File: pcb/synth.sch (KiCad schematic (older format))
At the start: 50 parts, among them J1 Conn_01x06, SW1 SW_Push, SW10 SW_Push, SW11 SW_Push, SW12 SW_Push, SW13 SW_Push, SW14 SW_Push, SW15 SW_Push, SW16 SW_Push, SW17 SW_Push, SW18 SW_Push, SW19 SW_Push, SW2 SW_Push, SW20 SW_Push, SW21 SW_Push, SW22 SW_Push, SW23 SW_Push, SW24 SW_Push, SW3 SW_Push, SW4 SW_Push, SW5 SW_Push, SW6 SW_Push, SW7 SW_Push, SW8 SW_Push, SW9 SW_Push, U1 STM32F407VGTx, Y1 Crystal_8

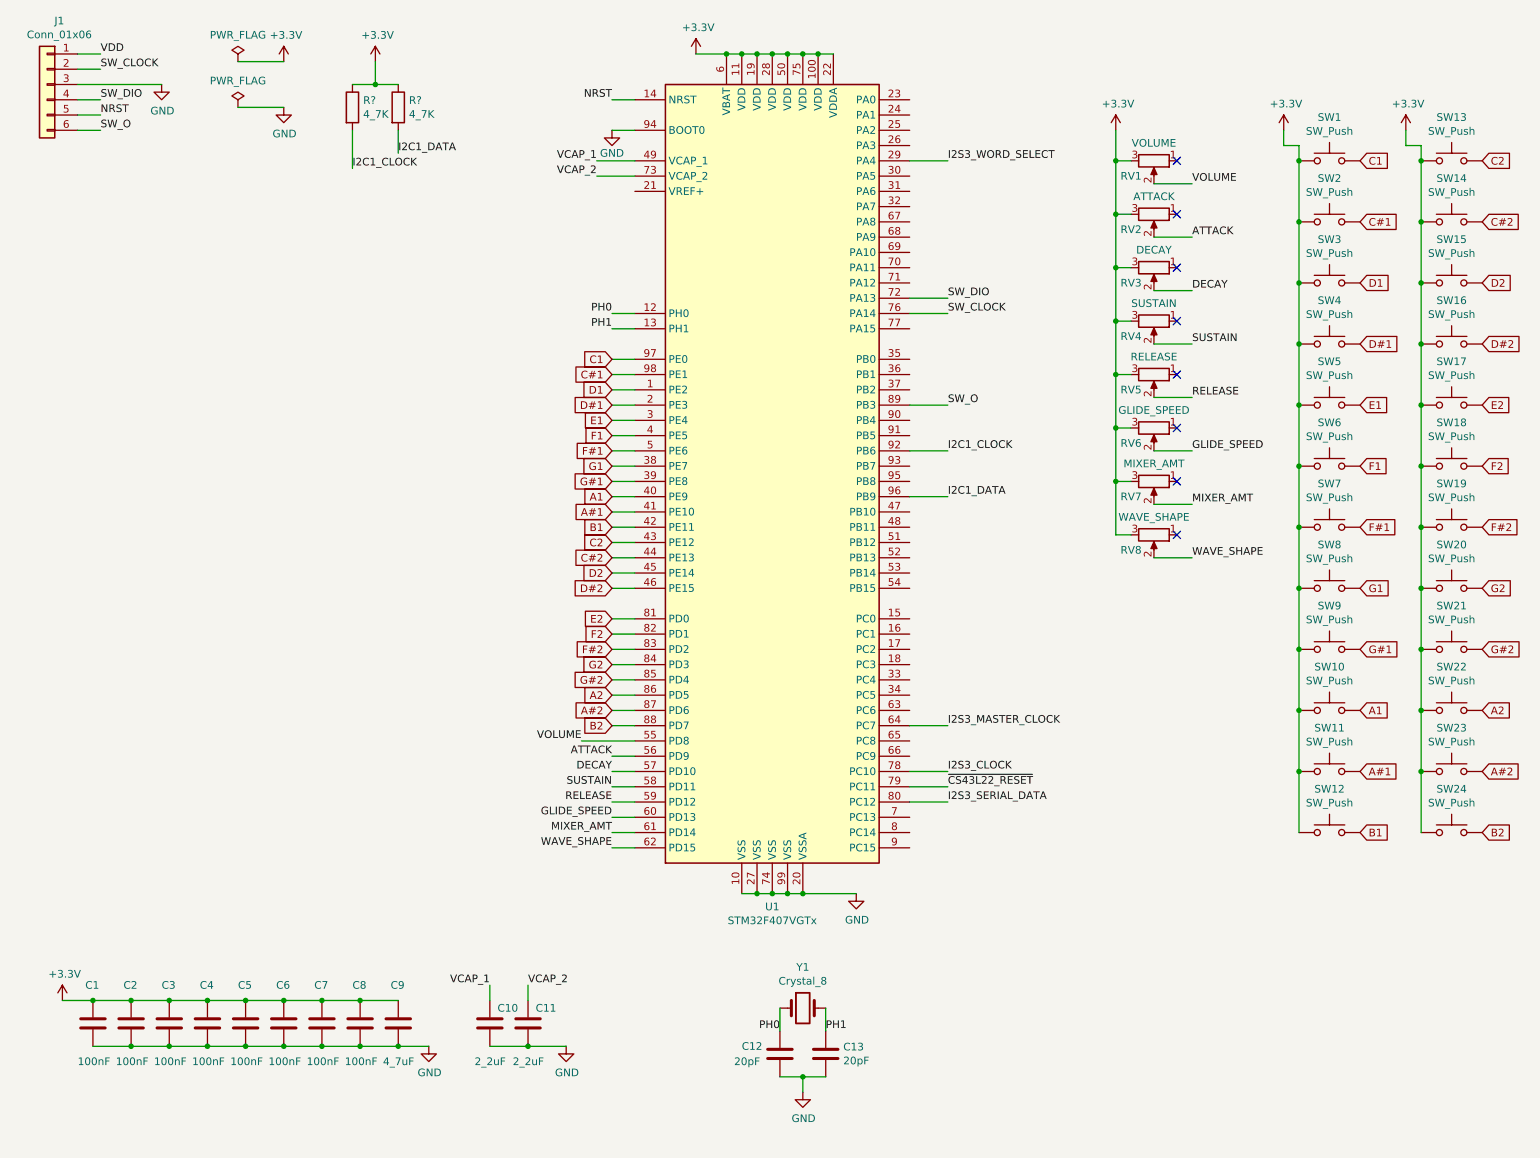
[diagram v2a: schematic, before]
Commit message: Add more buttons, and connect SWD VDD to 3.3V.
Also set some cap and resistor values.
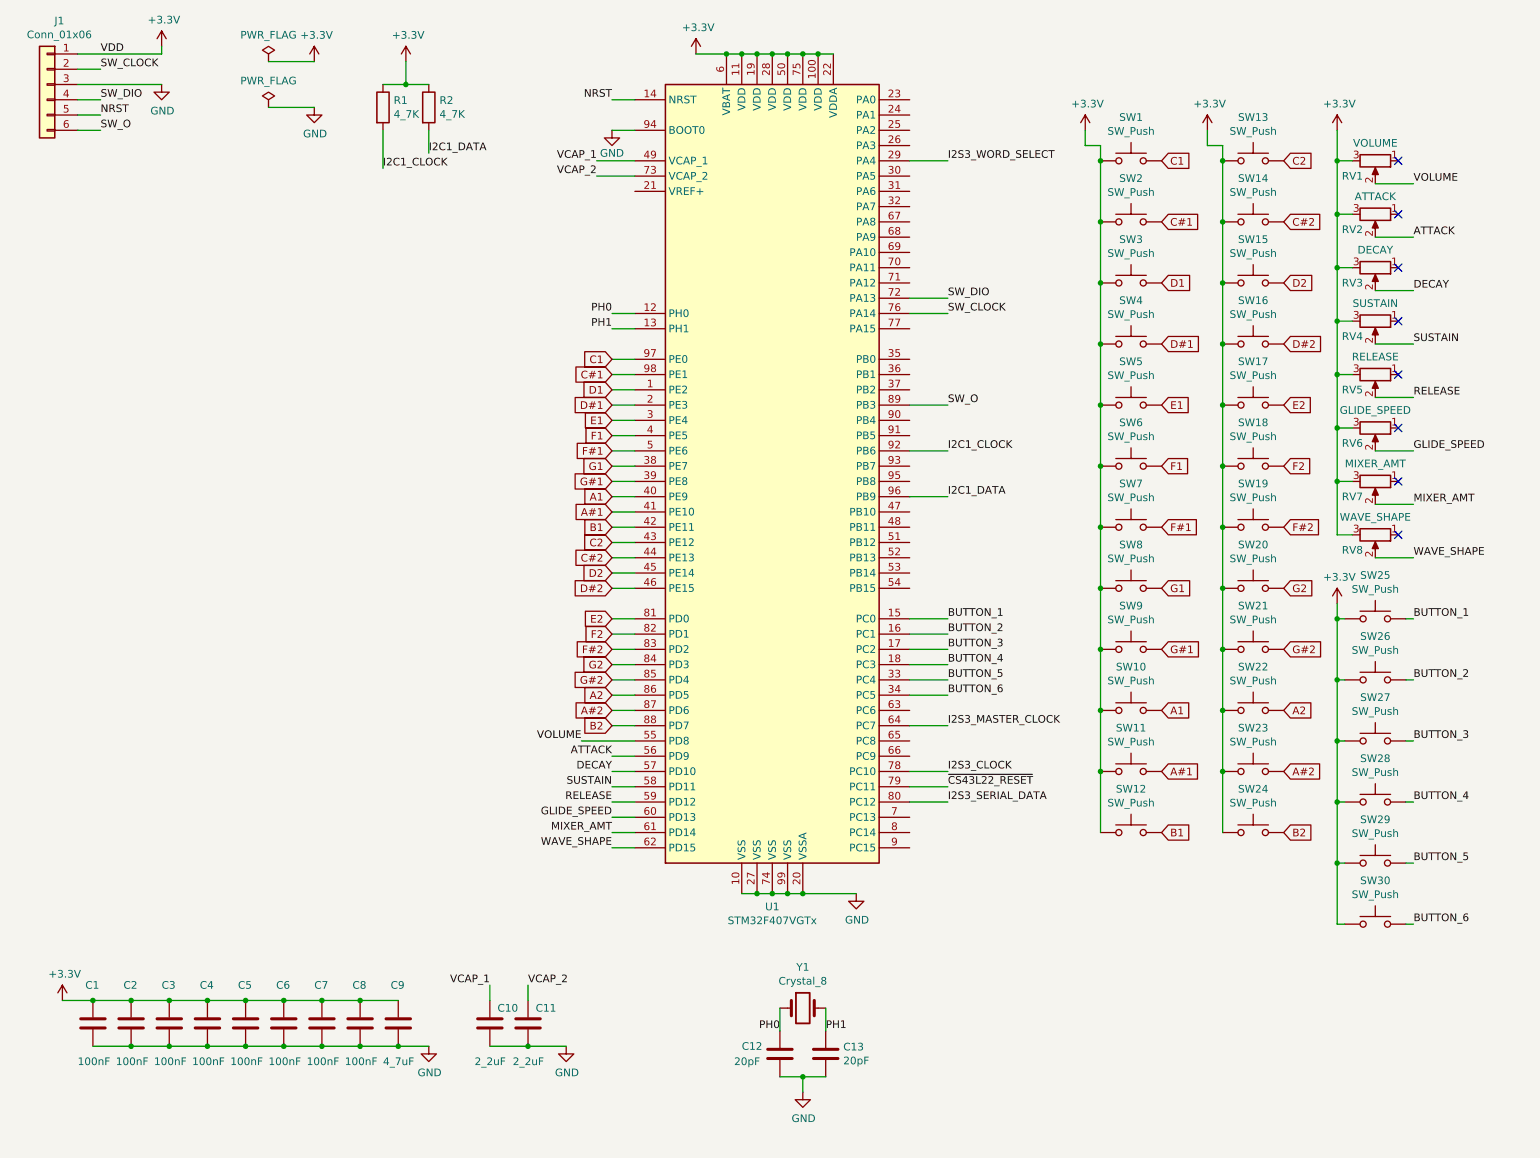
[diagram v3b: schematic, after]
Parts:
- added SW25, SW26, SW27, SW28, SW29, SW30: SW_Push, symbol Switch:SW_Push
- gave numbers to parts that had none: 2
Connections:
- net VDD is gone; now on net +3V3: J1.1 (Pin_1)
- net +3V3: now also SW25.1, SW26.1, SW27.1, SW28.1, SW29.1, SW30.1
- net BUTTON_1: now reaches U1.15 (PC0)
- net BUTTON_1: now also SW25.2
- net BUTTON_2: now reaches U1.16 (PC1)
- net BUTTON_2: now also SW26.2
- net BUTTON_3: now reaches U1.17 (PC2)
- net BUTTON_3: now also SW27.2
- net BUTTON_4: now reaches U1.18 (PC3)
- net BUTTON_4: now also SW28.2
- net BUTTON_5: now reaches U1.33 (PC4)
- net BUTTON_5: now also SW29.2
- net BUTTON_6: now reaches U1.34 (PC5)
- net BUTTON_6: now also SW30.2
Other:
- moved on the sheet: R1, R2, RV1, RV2, RV3, RV4, RV5, RV6, RV7, RV8, SW1, SW10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

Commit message: Add voltage regulator, barrel jack.
Also associated somewhat arbitrary footprints with components.
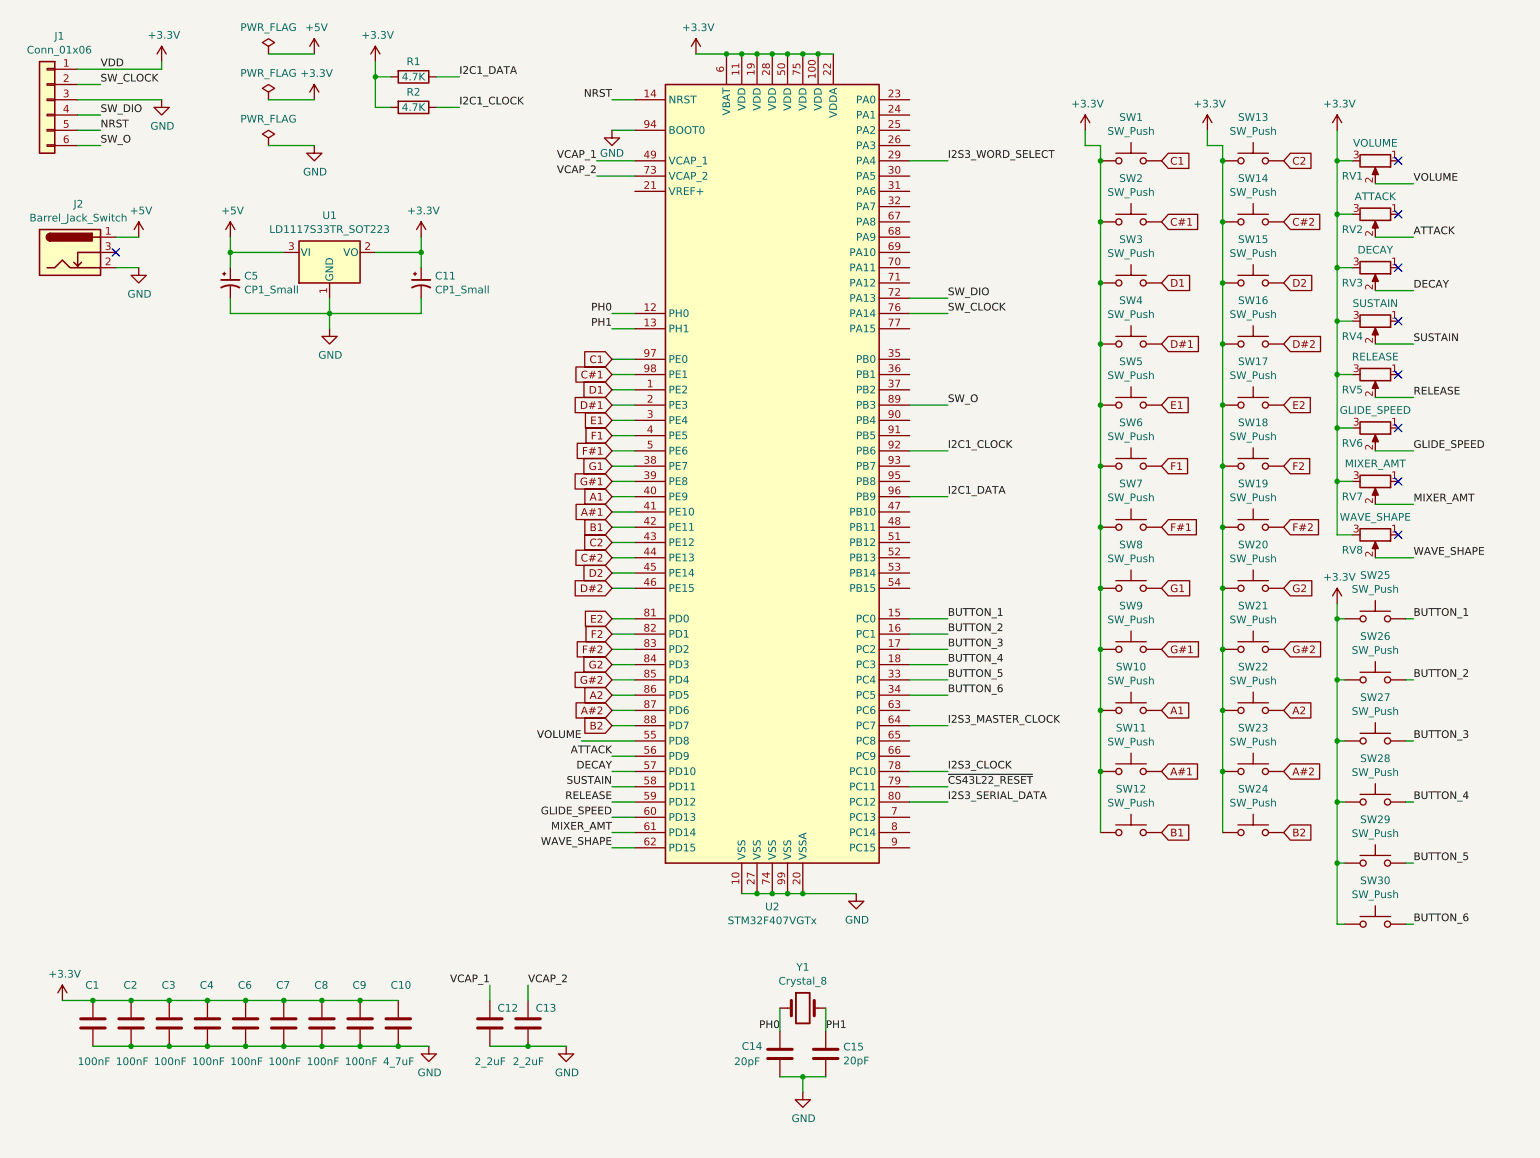
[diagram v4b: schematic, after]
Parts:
- added C11, C5: CP1_Small, symbol Device:CP1_Small
- added J2: Barrel_Jack_Switch, Connector_BarrelJack:BarrelJack_CUI_PJ-063AH_Horizontal, symbol Connector:Barrel_Jack_Switch
- added U1: LD1117S33TR_SOT223, Package_TO_SOT_SMD:SOT-223-3_TabPin2, symbol Regulator_Linear:LD1117S33TR_SOT223
- C1, C2, C3, C4: footprint (none) -> Capacitor_THT:CP_Axial_L11.0mm_D8.0mm_P15.00mm_Horizontal
- C10: renamed from C9; footprint (none) -> Capacitor_THT:CP_Axial_L11.0mm_D8.0mm_P15.00mm_Horizontal
- C12: renamed from C10; footprint (none) -> Capacitor_THT:CP_Axial_L11.0mm_D8.0mm_P15.00mm_Horizontal
- C13: renamed from C11; footprint (none) -> Capacitor_THT:CP_Axial_L11.0mm_D8.0mm_P15.00mm_Horizontal
- C14: renamed from C12; footprint (none) -> Capacitor_THT:CP_Axial_L11.0mm_D8.0mm_P15.00mm_Horizontal
- C15: renamed from C13; footprint (none) -> Capacitor_THT:CP_Axial_L11.0mm_D8.0mm_P15.00mm_Horizontal
- C6: renamed from C5; footprint (none) -> Capacitor_THT:CP_Axial_L11.0mm_D8.0mm_P15.00mm_Horizontal
- C7: renamed from C6; footprint (none) -> Capacitor_THT:CP_Axial_L11.0mm_D8.0mm_P15.00mm_Horizontal
- C8: renamed from C7; footprint (none) -> Capacitor_THT:CP_Axial_L11.0mm_D8.0mm_P15.00mm_Horizontal
- C9: renamed from C8; footprint (none) -> Capacitor_THT:CP_Axial_L11.0mm_D8.0mm_P15.00mm_Horizontal
- J1: footprint (none) -> Connector_PinHeader_2.54mm:PinHeader_1x06_P2.54mm_Vertical
- R1, R2: value 4_7K -> 4.7K; footprint (none) -> Resistor_THT:R_Axial_DIN0207_L6.3mm_D2.5mm_P2.54mm_Vertical
- RV1, RV2, RV3, RV4, RV5, RV6, RV7, RV8: footprint (none) -> Potentiometer_THT:Potentiometer_Bourns_3005_Horizontal
- SW1, SW10, SW11, SW12, SW13, SW14, SW15, SW16, SW17, SW18, SW19, SW2, SW20, SW21, SW22, SW23, SW24, SW25, SW26, SW27, SW28, SW29, SW3, SW30, SW4, SW5, SW6, SW7, SW8, SW9: footprint (none) -> Button_Switch_THT:SW_PUSH_6mm
- Y1: footprint (none) -> Crystal:Crystal_AT310_D3.0mm_L10.0mm_Horizontal
- renumbered U1 to U2
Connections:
- net +3V3: now also R1.2, R2.2, C11.1, U1.2 (VO); no longer R1.1, R2.1
- net GND: now also C11.2, C5.2, J2.2, U1.1 (GND)
- net I2C1_CLOCK: now also R2.1; no longer R1.2
- net I2C1_DATA: now also R1.1; no longer R2.2
- new net +5V: C5.1, J2.1, U1.3 (VI)
- no-connect marks 8 -> 9
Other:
- moved on the sheet: J1, R1

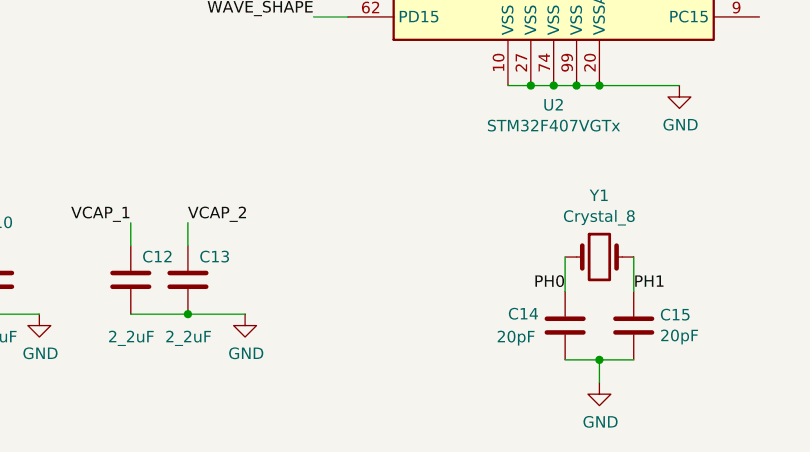
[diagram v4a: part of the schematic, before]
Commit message: Hook up VREF to ground through a 1uF and .1uF cap.
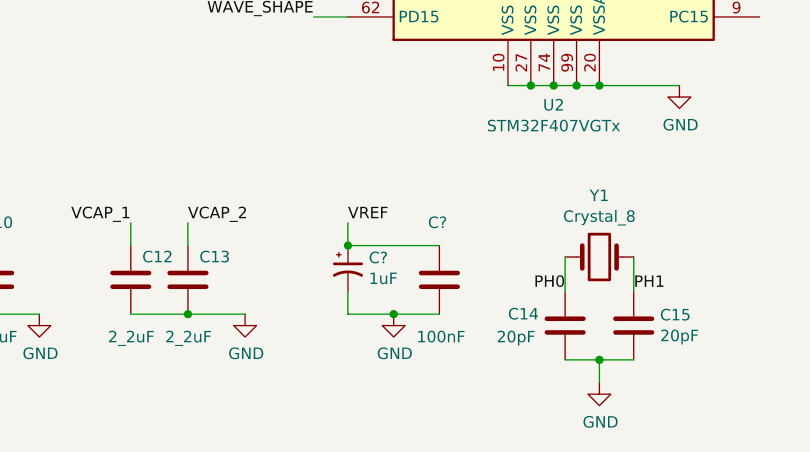
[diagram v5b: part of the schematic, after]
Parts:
- added C?: 1uF, symbol Device:CP1_Small
- added C?: 100nF, Capacitor_THT:CP_Axial_L11.0mm_D8.0mm_P15.00mm_Horizontal, symbol Device:C
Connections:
- net GND: now also C?.2, C?.2
- new net VREF: C?.1, C?.1
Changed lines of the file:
@@
 Wire Wire Line
 	3250 1150 3400 1150
+$Comp
+L Device:CP1_Small C?
+U 1 1 5C9898EA
+P 4550 7100
+F 0 "C?" H 4641 7146 50  0000 L CNN
+F 1 "1uF" H 4641 7055 50  0000 L CNN
+F 2 "" H 4550 7100 50  0001 C CNN
+F 3 "~" H 4550 7100 50  0001 C CNN
+	1    4550 7100
+	1    0    0    -1
+$EndComp
+$Comp
+L Device:C C?
+U 1 1 5C989ADA
+P 4950 7150
+F 0 "C?" H 4900 7400 50  0000 L CNN
+F 1 "100nF" H 4850 6900 50  0000 L CNN
+F 2 "Capacitor_THT:CP_Axial_L11.0mm_D8.0mm_P15.00mm_Horizontal" H 4988 7000 50  0001 C CNN
+F 3 "~" H 4950 7150 50  0001 C CNN
+	1    4950 7150
+	1    0    0    -1
+$EndComp
+Text Label 4550 6900 0    50   ~ 0
+VREF
+Wire Wire Line
+	4550 6900 4550 7000
+Connection ~ 4550 7000
+Wire Wire Line
+	4550 7200 4550 7300
+Wire Wire Line
+	4550 7300 4750 7300
+$Comp
+L power:GND #PWR?
+U 1 1 5C9B9001
+P 4750 7300
+F 0 "#PWR?" H 4750 7050 50  0001 C CNN
+F 1 "GND" H 4755 7127 50  0000 C CNN
+F 2 "" H 4750 7300 50  0001 C CNN
+F 3 "" H 4750 7300 50  0001 C CNN
+	1    4750 7300
+	1    0    0    -1
+$EndComp
+Connection ~ 4750 7300
+Wire Wire Line
+	4750 7300 4950 7300
+Wire Wire Line
+	4550 7000 4950 7000
 $EndSCHEMATC

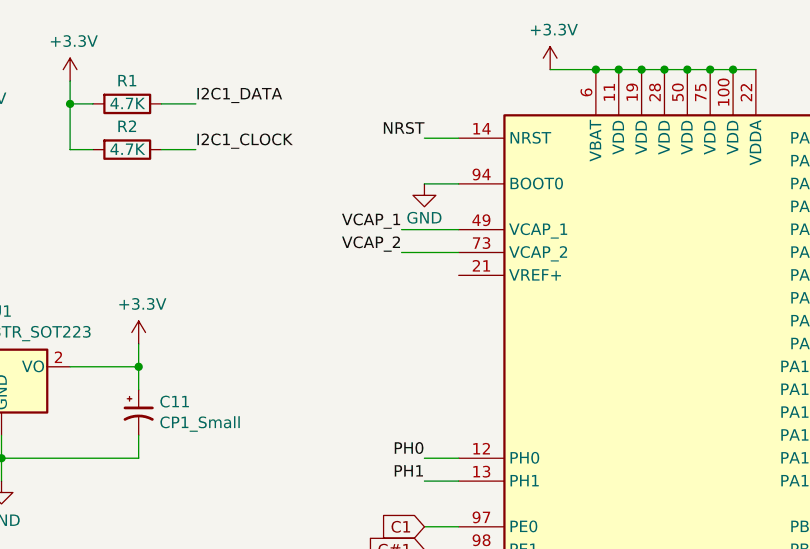
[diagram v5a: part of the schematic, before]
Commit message: Connect the VREF pin to the VREF net.
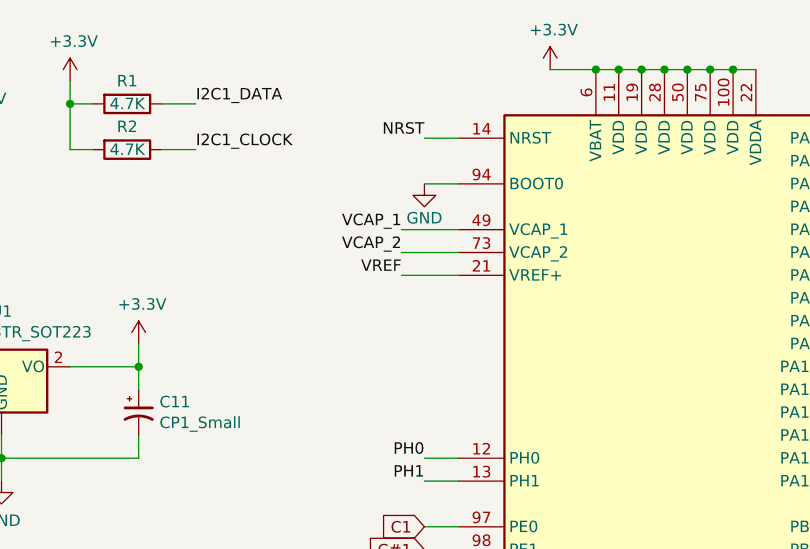
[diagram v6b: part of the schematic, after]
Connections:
- net VREF: now also U2.21 (VREF+)
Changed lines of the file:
@@
 Wire Wire Line
 	4550 7000 4950 7000
+Text Label 4300 1700 2    50   ~ 0
+VREF
+Wire Wire Line
+	4300 1700 4550 1700
 $EndSCHEMATC
